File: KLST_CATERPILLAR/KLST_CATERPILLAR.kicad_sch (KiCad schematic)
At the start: 12 parts

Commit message: changed project name
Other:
- title: KLST_PANDA -> KLST_CATERPILLAR
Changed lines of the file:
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@@
 	(paper "A3")
 	(title_block
-		(title "KLST_PANDA")
+		(title "KLST_CATERPILLAR")
 		(date "2023-08-19")
 		(rev "V1.0")
@@
 		)
 		(instances
-			(project "KLST_PANDA"
+			(project "KLST_CATERPILLAR"
 				(path "/b4513875-4c57-4720-bcc5-43ead67fe18f"
 					(reference "R6")
@@
 		)
 		(instances
-			(project "KLST_PANDA"
+			(project "KLST_CATERPILLAR"
 				(path "/b4513875-4c57-4720-bcc5-43ead67fe18f"
 					(reference "#PWR04")
@@
 		)
 		(instances
-			(project "KLST_PANDA"
+			(project "KLST_CATERPILLAR"
 				(path "/b4513875-4c57-4720-bcc5-43ead67fe18f"
 					(reference "H4")
@@
 		)
 		(instances
-			(project "KLST_PANDA"
+			(project "KLST_CATERPILLAR"
 				(path "/b4513875-4c57-4720-bcc5-43ead67fe18f"
 					(reference "R2")
@@
 		)
 		(instances
-			(project "KLST_PANDA"
+			(project "KLST_CATERPILLAR"
 				(path "/b4513875-4c57-4720-bcc5-43ead67fe18f"
 					(reference "D1")
@@
 		)
 		(instances
-			(project "KLST_PANDA"
+			(project "KLST_CATERPILLAR"
 				(path "/b4513875-4c57-4720-bcc5-43ead67fe18f"
 					(reference "H3")
@@
 		)
 		(instances
-			(project "KLST_PANDA"
+			(project "KLST_CATERPILLAR"
 				(path "/b4513875-4c57-4720-bcc5-43ead67fe18f"
 					(reference "#PWR02")
@@
 		)
 		(instances
-			(project "KLST_PANDA"
+			(project "KLST_CATERPILLAR"
 				(path "/b4513875-4c57-4720-bcc5-43ead67fe18f"
 					(reference "R3")
@@
 		)
 		(instances
-			(project "KLST_PANDA"
+			(project "KLST_CATERPILLAR"
 				(path "/b4513875-4c57-4720-bcc5-43ead67fe18f"
 					(reference "D2")
@@
 		)
 		(instances
-			(project "KLST_PANDA"
+			(project "KLST_CATERPILLAR"
 				(path "/b4513875-4c57-4720-bcc5-43ead67fe18f"
 					(reference "H2")
@@
 		)
 		(instances
-			(project "KLST_PANDA"
+			(project "KLST_CATERPILLAR"
 				(path "/b4513875-4c57-4720-bcc5-43ead67fe18f"
 					(reference "R1")
@@
 		)
 		(instances
-			(project "KLST_PANDA"
+			(project "KLST_CATERPILLAR"
 				(path "/b4513875-4c57-4720-bcc5-43ead67fe18f"
 					(reference "R4")
@@
 		)
 		(instances
-			(project "KLST_PANDA"
+			(project "KLST_CATERPILLAR"
 				(path "/b4513875-4c57-4720-bcc5-43ead67fe18f"
 					(reference "R5")
@@
 		)
 		(instances
-			(project "KLST_PANDA"
+			(project "KLST_CATERPILLAR"
 				(path "/b4513875-4c57-4720-bcc5-43ead67fe18f"
 					(reference "H1")
@@
 		)
 		(instances
-			(project "KLST_PANDA"
+			(project "KLST_CATERPILLAR"
 				(path "/b4513875-4c57-4720-bcc5-43ead67fe18f"
 					(reference "#PWR01")
@@
 		)
 		(instances
-			(project "KLST_PANDA"
+			(project "KLST_CATERPILLAR"
 				(path "/b4513875-4c57-4720-bcc5-43ead67fe18f"
 					(reference "#PWR03")
@@
 		)
 		(instances
-			(project "KLST_PANDA"
+			(project "KLST_CATERPILLAR"
 				(path "/b4513875-4c57-4720-bcc5-43ead67fe18f"
 					(page "16")
@@
 		)
 		(instances
-			(project "KLST_PANDA"
+			(project "KLST_CATERPILLAR"
 				(path "/b4513875-4c57-4720-bcc5-43ead67fe18f"
 					(page "23")
@@
 		)
 		(instances
-			(project "KLST_PANDA"
+			(project "KLST_CATERPILLAR"
 				(path "/b4513875-4c57-4720-bcc5-43ead67fe18f"
 					(page "20")
@@
 		)
 		(instances
-			(project "KLST_PANDA"
+			(project "KLST_CATERPILLAR"
 				(path "/b4513875-4c57-4720-bcc5-43ead67fe18f"
 					(page "4")
@@
 		)
 		(instances
-			(project "KLST_PANDA"
+			(project "KLST_CATERPILLAR"
 				(path "/b4513875-4c57-4720-bcc5-43ead67fe18f"
 					(page "19")
@@
 		)
 		(instances
-			(project "KLST_PANDA"
+			(project "KLST_CATERPILLAR"
 				(path "/b4513875-4c57-4720-bcc5-43ead67fe18f"
 					(page "10")
@@
 		)
 		(instances
-			(project "KLST_PANDA"
+			(project "KLST_CATERPILLAR"
 				(path "/b4513875-4c57-4720-bcc5-43ead67fe18f"
 					(page "6")
@@
 		)
 		(instances
-			(project "KLST_PANDA"
+			(project "KLST_CATERPILLAR"
 				(path "/b4513875-4c57-4720-bcc5-43ead67fe18f"
 					(page "25")
@@
 		)
 		(instances
-			(project "KLST_PANDA"
+			(project "KLST_CATERPILLAR"
 				(path "/b4513875-4c57-4720-bcc5-43ead67fe18f"
 					(page "18")
@@
 		)
 		(instances
-			(project "KLST_PANDA"
+			(project "KLST_CATERPILLAR"
 				(path "/b4513875-4c57-4720-bcc5-43ead67fe18f"
 					(page "7")
@@
 		)
 		(instances
-			(project "KLST_PANDA"
+			(project "KLST_CATERPILLAR"
 				(path "/b4513875-4c57-4720-bcc5-43ead67fe18f"
 					(page "17")
@@
 		)
 		(instances
-			(project "KLST_PANDA"
+			(project "KLST_CATERPILLAR"
 				(path "/b4513875-4c57-4720-bcc5-43ead67fe18f"
 					(page "3")
@@
 		)
 		(instances
-			(project "KLST_PANDA"
+			(project "KLST_CATERPILLAR"
 				(path "/b4513875-4c57-4720-bcc5-43ead67fe18f"
 					(page "5")
@@
 		)
 		(instances
-			(project "KLST_PANDA"
+			(project "KLST_CATERPILLAR"
 				(path "/b4513875-4c57-4720-bcc5-43ead67fe18f"
 					(page "2")
@@
 		)
 		(instances
-			(project "KLST_PANDA"
+			(project "KLST_CATERPILLAR"
 				(path "/b4513875-4c57-4720-bcc5-43ead67fe18f"
 					(page "13")
@@
 		)
 		(instances
-			(project "KLST_PANDA"
+			(project "KLST_CATERPILLAR"
 				(path "/b4513875-4c57-4720-bcc5-43ead67fe18f"
 					(page "24")

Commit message: reduced modules
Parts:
- removed H1, H2, H3, H4: M3 Mounting Hole, MountingHole:MountingHole_3.2mm_M3_Pad_Via, symbol Mechanical:MountingHole_Pad
- removed R5, R6: 2.2K, Resistor_SMD:R_0402_1005Metric, symbol Device:R_Small
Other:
- removed sheet ADC_DAC
- removed sheet MIDI_analog
- removed sheet battery
- removed sheet buttons_keys
- removed sheet display
- removed sheet external_memory
- removed sheet rotary_encoders
- note removed: "I2C USR"
- note removed: "MOUNTING HOLES"

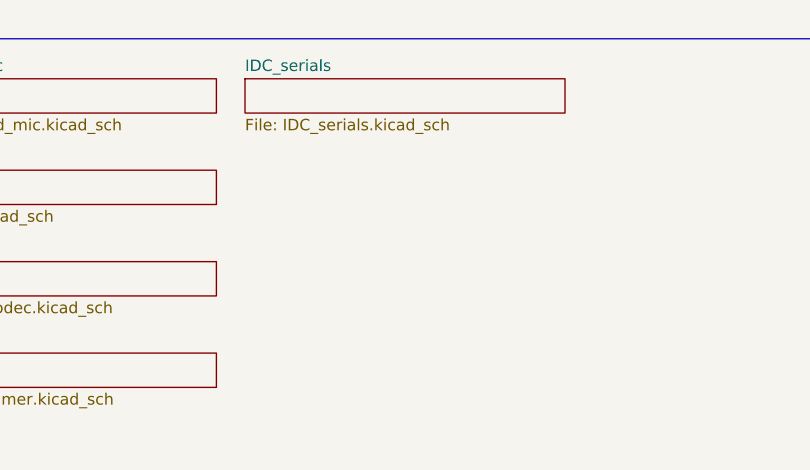
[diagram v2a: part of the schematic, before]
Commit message: added GPIOs
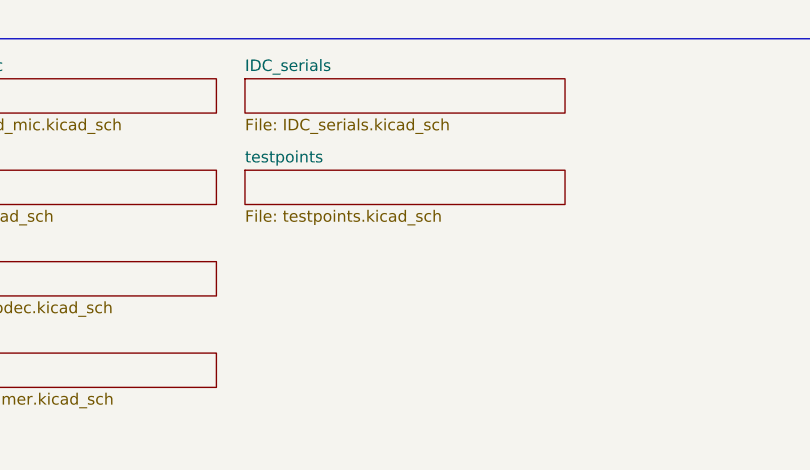
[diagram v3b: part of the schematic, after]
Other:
- added sheet testpoints (testpoints.kicad_sch)
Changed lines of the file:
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@@
+	)
+	(sheet
+		(at 133.985 29.845)
+		(size 35.56 3.81)
+		(fields_autoplaced yes)
+		(stroke
+			(width 0.1524)
+			(type solid)
+		)
+		(fill
+			(color 0 0 0 0.0000)
+		)
+		(property "Sheetname" "testpoints"
+			(at 133.985 29.1334 0)
+			(effects
+				(font
+					(size 1.27 1.27)
+				)
+				(justify left bottom)
+			)
+		)
+		(property "Sheetfile" "testpoints.kicad_sch"
+			(at 133.985 34.2396 0)
+			(effects
+				(font
+					(size 1.27 1.27)
+				)
+				(justify left top)
+			)
+		)
+		(instances
+			(project "KLST_CATERPILLAR"
+				(path "/b4513875-4c57-4720-bcc5-43ead67fe18f"
+					(page "12")
+				)
+			)
+		)
 	)
 	(sheet
